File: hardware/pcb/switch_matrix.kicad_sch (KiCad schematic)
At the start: 32 parts, among them SW1 SW_Push, SW10 SW_Push, SW11 SW_Push, SW12 SW_Push, SW13 SW_Push, SW14 SW_Push, SW15 SW_Push, SW16 SW_Push, SW2 SW_Push, SW3 SW_Push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

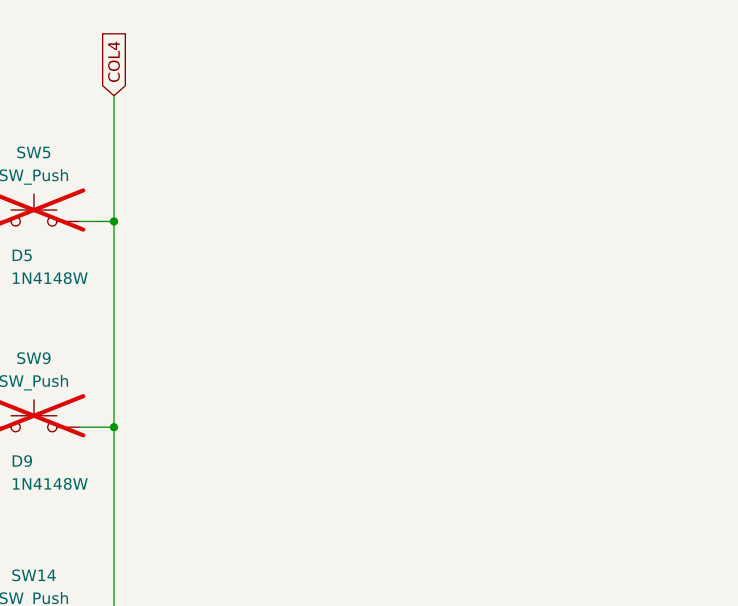
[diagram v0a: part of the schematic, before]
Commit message: Better EMC and ESD safety
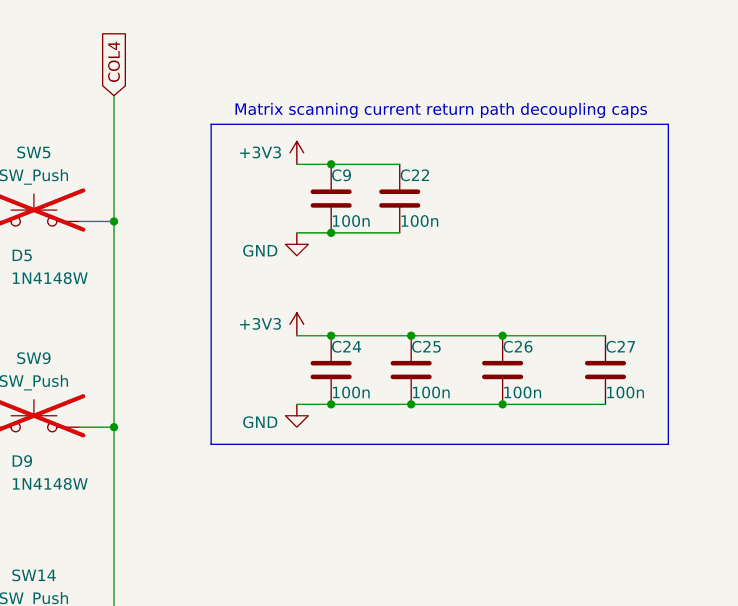
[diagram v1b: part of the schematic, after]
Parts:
- added C22, C24, C25, C26, C27, C9: 100n, Capacitor_SMD:C_0402_1005Metric, symbol Device:C
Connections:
- new net +3V3: C22.1, C24.1, C25.1, C26.1, C27.1, C9.1
- new net GND: C22.2, C24.2, C25.2, C26.2, C27.2, C9.2
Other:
- note added: "Matrix scanning current return path decoupling caps"

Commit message: Version 1.5
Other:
- moved on the sheet: C22, C24, C25, C26, C27, C9, D1, D10, D11, D12, D13, D14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

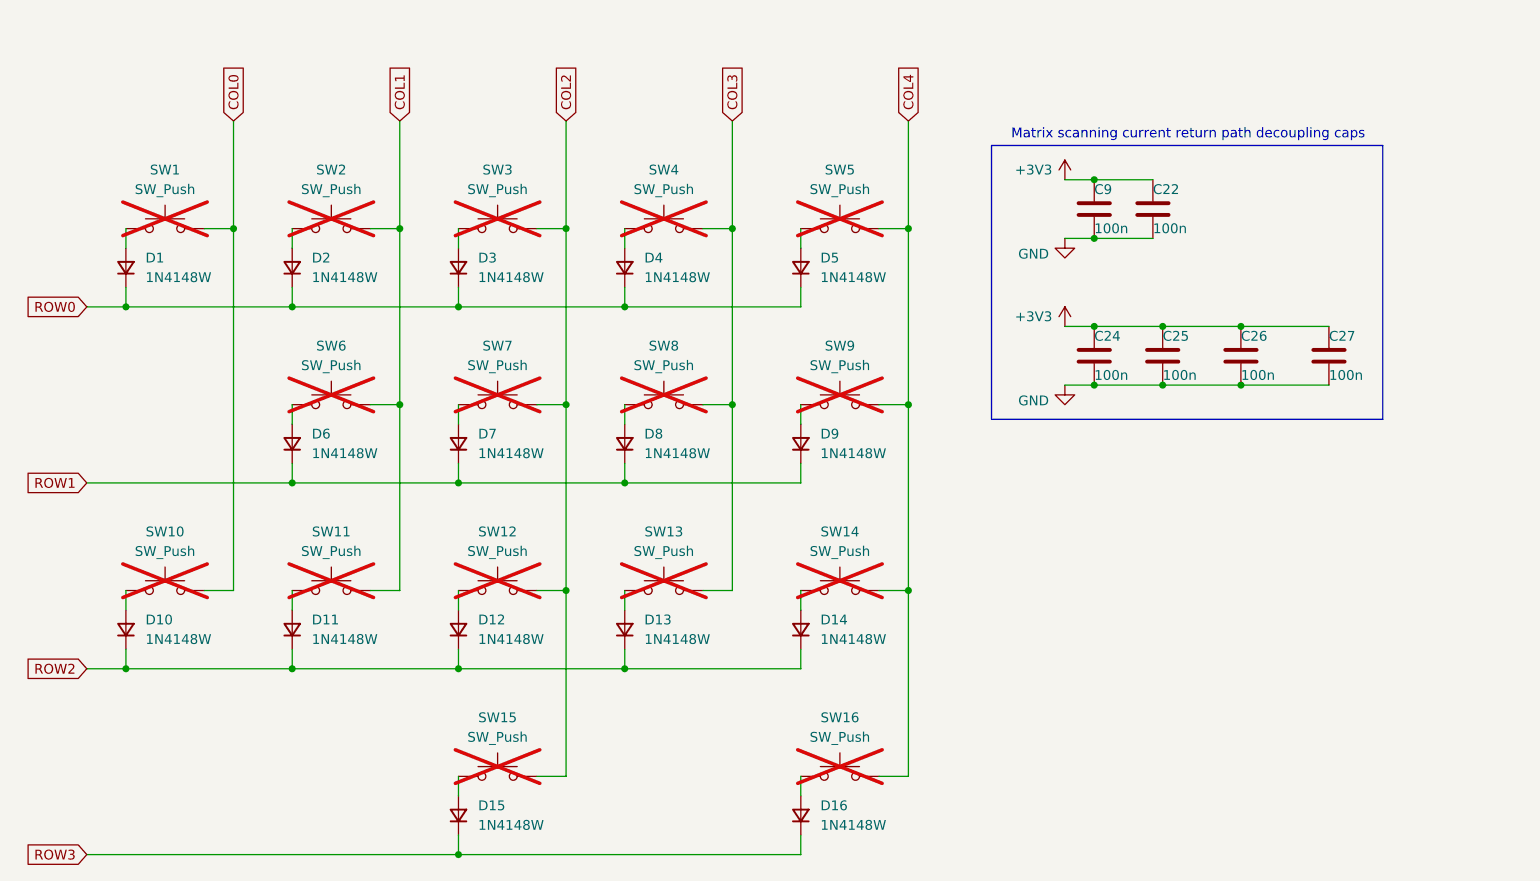
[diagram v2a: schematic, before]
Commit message: Hotswap sockets and fw improvements
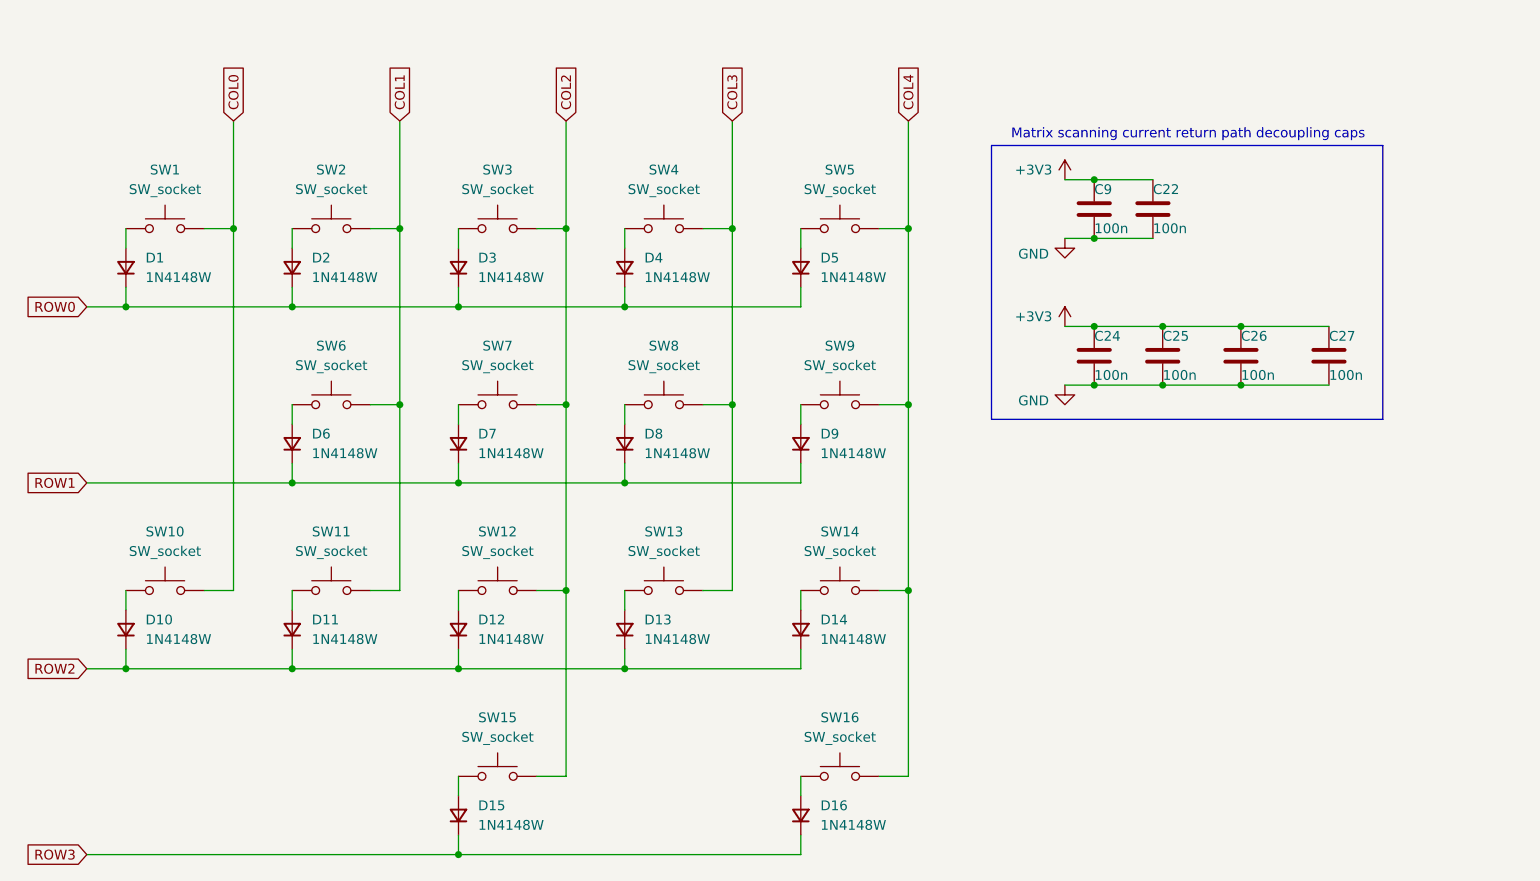
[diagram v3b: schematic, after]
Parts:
- SW1, SW10, SW11, SW12, SW13, SW14, SW15, SW16, SW2, SW3, SW4, SW5, SW6, SW7, SW8, SW9: value SW_Push -> SW_socket; footprint key-switches:SW_Gateron_LowProfile_THT -> mathboard:SW_Gateron_LowProfile_THT_hotswap; now fitted
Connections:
- net COL0: now also SW10.1; no longer SW10.2
- net COL4: now also SW16.1; no longer SW16.2
- net at D10.2 (A): now also SW10.2; no longer SW10.1
- net at D16.2 (A): now also SW16.2; no longer SW16.1
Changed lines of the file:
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@@
 		(in_bom yes)
 		(on_board yes)
-		(dnp yes)
+		(dnp no)
 		(fields_autoplaced yes)
 		(property "Reference" "SW11"
@@
 			)
 		)
-		(property "Value" "SW_Push"
+		(property "Value" "SW_socket"
 			(at 107.95 104.14 0)
 			(effects
@@
 			)
 		)
-		(property "Footprint" "key-switches:SW_Gateron_LowProfile_THT"
+		(property "Footprint" "mathboard:SW_Gateron_LowProfile_THT_hotswap"
 			(at 107.95 104.14 0)
 			(effects
@@
 		(in_bom yes)
 		(on_board yes)
-		(dnp yes)
+		(dnp no)
 		(fields_autoplaced yes)
 		(property "Reference" "SW2"
@@
 			)
 		)
-		(property "Value" "SW_Push"
+		(property "Value" "SW_socket"
 			(at 107.95 57.15 0)
 			(effects
@@
 			)
 		)
-		(property "Footprint" "key-switches:SW_Gateron_LowProfile_THT"
+		(property "Footprint" "mathboard:SW_Gateron_LowProfile_THT_hotswap"
 			(at 107.95 57.15 0)
 			(effects
@@
 		(in_bom yes)
 		(on_board yes)
-		(dnp yes)
+		(dnp no)
 		(fields_autoplaced yes)
 		(property "Reference" "SW13"
@@
 			)
 		)
-		(property "Value" "SW_Push"
+		(property "Value" "SW_socket"
 			(at 151.13 104.14 0)
 			(effects
@@
 			)
 		)
-		(property "Footprint" "key-switches:SW_Gateron_LowProfile_THT"
+		(property "Footprint" "mathboard:SW_Gateron_LowProfile_THT_hotswap"
 			(at 151.13 104.14 0)
 			(effects
@@
 		(in_bom yes)
 		(on_board yes)
-		(dnp yes)
+		(dnp no)
 		(fields_autoplaced yes)
 		(property "Reference" "SW14"
@@
 			)
 		)
-		(property "Value" "SW_Push"
+		(property "Value" "SW_socket"
 			(at 173.99 104.14 0)
 			(effects
@@
 			)
 		)
-		(property "Footprint" "key-switches:SW_Gateron_LowProfile_THT"
+		(property "Footprint" "mathboard:SW_Gateron_LowProfile_THT_hotswap"
 			(at 173.99 104.14 0)
 			(effects
@@
 		(in_bom yes)
 		(on_board yes)
-		(dnp yes)
+		(dnp no)
 		(fields_autoplaced yes)
 		(property "Reference" "SW8"
@@
 			)
 		)
-		(property "Value" "SW_Push"
+		(property "Value" "SW_socket"
 			(at 151.13 80.01 0)
 			(effects
@@
 			)
 		)
-		(property "Footprint" "key-switches:SW_Gateron_LowProfile_THT"
+		(property "Footprint" "mathboard:SW_Gateron_LowProfile_THT_hotswap"
 			(at 151.13 80.01 0)
 			(effects
@@
 		(lib_id "Switch:SW_Push")
 		(at 86.36 109.22 0)
+		(mirror y)
 		(unit 1)
 		(exclude_from_sim no)
 		(in_bom yes)
 		(on_board yes)
-		(dnp yes)
-		(fields_autoplaced yes)
+		(dnp no)
 		(property "Reference" "SW10"
 			(at 86.36 101.6 0)
@@
 			)
 		)
-		(property "Value" "SW_Push"
+		(property "Value" "SW_socket"
 			(at 86.36 104.14 0)
 			(effects
@@
 			)
 		)
-		(property "Footprint" "key-switches:SW_Gateron_LowProfile_THT"
+		(property "Footprint" "mathboard:SW_Gateron_LowProfile_THT_hotswap"
 			(at 86.36 104.14 0)
 			(effects
@@
 		(in_bom yes)
 		(on_board yes)
-		(dnp yes)
+		(dnp no)
 		(fields_autoplaced yes)
 		(property "Reference" "SW1"
@@
 			)
 		)
-		(property "Value" "SW_Push"
+		(property "Value" "SW_socket"
 			(at 86.36 57.15 0)
 			(effects
@@
 			)
 		)
-		(property "Footprint" "key-switches:SW_Gateron_LowProfile_THT"
+		(property "Footprint" "mathboard:SW_Gateron_LowProfile_THT_hotswap"
 			(at 86.36 57.15 0)
 			(effects
@@
 		(lib_id "Switch:SW_Push")
 		(at 173.99 133.35 0)
+		(mirror y)
 		(unit 1)
 		(exclude_from_sim no)
 		(in_bom yes)
 		(on_board yes)
-		(dnp yes)
-		(fields_autoplaced yes)
+		(dnp no)
 		(property "Reference" "SW16"
 			(at 173.99 125.73 0)
@@
 			)
 		)
-		(property "Value" "SW_Push"
+		(property "Value" "SW_socket"
 			(at 173.99 128.27 0)
 			(effects
@@
 			)
 		)
-		(property "Footprint" "key-switches:SW_Gateron_LowProfile_THT"
+		(property "Footprint" "mathboard:SW_Gateron_LowProfile_THT_hotswap"
 			(at 173.99 128.27 0)
 			(effects
@@
 		(in_bom yes)
 		(on_board yes)
-		(dnp yes)
+		(dnp no)
 		(fields_autoplaced yes)
 		(property "Reference" "SW6"
@@
 			)
 		)
-		(property "Value" "SW_Push"
+		(property "Value" "SW_socket"
 			(at 107.95 80.01 0)
 			(effects
@@
 			)
 		)
-		(property "Footprint" "key-switches:SW_Gateron_LowProfile_THT"
+		(property "Footprint" "mathboard:SW_Gateron_LowProfile_THT_hotswap"
 			(at 107.95 80.01 0)
 			(effects
@@
 		(in_bom yes)
 		(on_board yes)
-		(dnp yes)
+		(dnp no)
 		(fields_autoplaced yes)
 		(property "Reference" "SW7"
@@
 			)
 		)
-		(property "Value" "SW_Push"
+		(property "Value" "SW_socket"
 			(at 129.54 80.01 0)
 			(effects
@@
 			)
 		)
-		(property "Footprint" "key-switches:SW_Gateron_LowProfile_THT"
+		(property "Footprint" "mathboard:SW_Gateron_LowProfile_THT_hotswap"
 			(at 129.54 80.01 0)
 			(effects
@@
 		(in_bom yes)
 		(on_board yes)
-		(dnp yes)
+		(dnp no)
 		(fields_autoplaced yes)
 		(property "Reference" "SW12"
@@
 			)
 		)
-		(property "Value" "SW_Push"
+		(property "Value" "SW_socket"
 			(at 129.54 104.14 0)
 			(effects
@@
 			)
 		)
-		(property "Footprint" "key-switches:SW_Gateron_LowProfile_THT"
+		(property "Footprint" "mathboard:SW_Gateron_LowProfile_THT_hotswap"
 			(at 129.54 104.14 0)
 			(effects
@@
 		(in_bom yes)
 		(on_board yes)
-		(dnp yes)
+		(dnp no)
 		(fields_autoplaced yes)
 		(property "Reference" "SW15"
@@
 			)
 		)
-		(property "Value" "SW_Push"
+		(property "Value" "SW_socket"
 			(at 129.54 128.27 0)
 			(effects
@@
 			)
 		)
-		(property "Footprint" "key-switches:SW_Gateron_LowProfile_THT"
+		(property "Footprint" "mathboard:SW_Gateron_LowProfile_THT_hotswap"
 			(at 129.54 128.27 0)
 			(effects
@@
 		(in_bom yes)
 		(on_board yes)
-		(dnp yes)
+		(dnp no)
 		(fields_autoplaced yes)
 		(property "Reference" "SW3"
@@
 			)
 		)
-		(property "Value" "SW_Push"
+		(property "Value" "SW_socket"
 			(at 129.54 57.15 0)
 			(effects
@@
 			)
 		)
-		(property "Footprint" "key-switches:SW_Gateron_LowProfile_THT"
+		(property "Footprint" "mathboard:SW_Gateron_LowProfile_THT_hotswap"
 			(at 129.54 57.15 0)
 			(effects
@@
 		(in_bom no)
 		(on_board yes)
-		(dnp yes)
+		(dnp no)
 		(fields_autoplaced yes)
 		(property "Reference" "SW4"
@@
 			)
 		)
-		(property "Value" "SW_Push"
+		(property "Value" "SW_socket"
 			(at 151.13 57.15 0)
 			(effects
@@
 			)
 		)
-		(property "Footprint" "key-switches:SW_Gateron_LowProfile_THT"
+		(property "Footprint" "mathboard:SW_Gateron_LowProfile_THT_hotswap"
 			(at 151.13 57.15 0)
 			(effects
@@
 		(in_bom yes)
 		(on_board yes)
-		(dnp yes)
+		(dnp no)
 		(fields_autoplaced yes)
 		(property "Reference" "SW5"
@@
 			)
 		)
-		(property "Value" "SW_Push"
+		(property "Value" "SW_socket"
 			(at 173.99 57.15 0)
 			(effects
@@
 			)
 		)
-		(property "Footprint" "key-switches:SW_Gateron_LowProfile_THT"
+		(property "Footprint" "mathboard:SW_Gateron_LowProfile_THT_hotswap"
 			(at 173.99 57.15 0)
 			(effects
@@
 		(in_bom yes)
 		(on_board yes)
-		(dnp yes)
+		(dnp no)
 		(fields_autoplaced yes)
 		(property "Reference" "SW9"
@@
 			)
 		)
-		(property "Value" "SW_Push"
+		(property "Value" "SW_socket"
 			(at 173.99 80.01 0)
 			(effects
@@
 			)
 		)
-		(property "Footprint" "key-switches:SW_Gateron_LowProfile_THT"
+		(property "Footprint" "mathboard:SW_Gateron_LowProfile_THT_hotswap"
 			(at 173.99 80.01 0)
 			(effects
